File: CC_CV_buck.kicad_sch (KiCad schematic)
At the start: 29 parts, among them Q1 TIP42C, Q2 AO3400A, Q3 MMBT3906, U1 OPA2197xD, U2 INA194, U3 AOZ6605PI-1

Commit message: configure gitignore
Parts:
- U3: footprint aoz6605:SO8_EP1_AOS-M -> AOZ6605PI_1:SO8_EP1_AOS-L
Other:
- note added: "tie EN to a switch or something"
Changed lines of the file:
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@@
+		)
+	)
+	(text "tie EN to a switch or something "
+		(exclude_from_sim no)
+		(at 36.83 28.702 0)
+		(effects
+			(font
+				(size 1.27 1.27)
+			)
 		)
 	)
@@
 			)
 		)
-		(property "Footprint" "aoz6605:SO8_EP1_AOS-M"
+		(property "Footprint" "AOZ6605PI_1:SO8_EP1_AOS-L"
 			(at 64.77 41.91 0)
 			(effects

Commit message: did a bunch of stuff
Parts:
- added C12: 100n, symbol Device:C
- added C13, C14, C15, C16, C17: tbd, symbol Device:C
- added R11, R12, R13, R14, R15: tbd, symbol Device:R_US
- added RV1, RV2: tbd, symbol Device:R_Potentiometer_US
- added SW1: SW_SPDT_312, symbol Switch:SW_SPDT_312
- C11: value tbd -> 150u
- C5: value C_Small -> 100n
- R1, R2: value R_Small_US -> tbd
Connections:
- net GND: now also R2.2, U1.4 (V-), C12.2, C13.2, C14.2, C15.2, C16.2, C17.2, R14.1
- net at C2.1, R3.1, U1.2 (-): now also R13.1, R14.2
- net at Q1.2 (C), R10.1: now also C10.1, C11.1
- net at Q1.3 (E): now also L1.2, R1.1, C13.1, C14.1, C15.1, R11.1
- net VSET: now reaches U1.3 (+)
- net at R1.2, R2.1: now also SW1.2 (C)
- net at U3.2 (EN), U3.3 (VIN): now also C16.1, C17.1
- net at U3.8 (FB): now also SW1.1 (B)
- net ISET: now reaches U1.5 (+)
- net at C3.1, R4.1, U1.6 (-): now also R15.2
- net at Q3.1 (B): now also R12.1
- net at Q3.2 (E): now also R11.2
- net at Q3.3 (C), R9.1: now also SW1.3 (A)
- net at U2.1: now also R15.1
- net at R10.4: now also R13.2
- net at U1.8 (V+): now also C12.1
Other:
- note added: "300 kHz BW"
- note added: "500 mV / A"
- note added: "CC"
- note added: "CV"
- note added: "Vdo = Vfb_buck*(R11/R9)+ Veb"
- note added: "todo: find connectors for input, buck and LDO output figure out pot voltage ranges finalize Vin (~13V) and Vcc for control loop design buck LEDs for power, and CC/CV figure out better way to disconnect LDO and buck find shunt"
- moved on the sheet: C1, C10, C11, C2, C3, C4, C5, C6, C7, C8, C9, D1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

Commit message: added block terminals
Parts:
- removed SW1: SW_SPDT_312, symbol Switch:SW_SPDT_312
- added J1, J2, J3: ~, symbol Connector:Screw_Terminal_01x02
- added R16, R17: 0, symbol Device:R_Small_US
- C9: value tbd -> 1u
- R11: value tbd -> 10k
- R12: value tbd -> 1k
- R9: value tbd -> 15k
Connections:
- net GND: now also J1.2 (Pin_2), J2.2 (Pin_2), J3.2 (Pin_2)
- net at U3.8 (FB): now also R16.1, R17.1
- net at R1.2, R2.1: now also R16.2
- net at Q3.3 (C), R9.1: now also R17.2
- net VOUT_BUCK: now reaches C13.1, C14.1, L1.2, R1.1, R11.1
- net VOUT_BUCK: now also J1.1 (Pin_1); no longer C15.1, Q1.3 (E)
- net VOUT_LDO: now reaches R10.4, R13.2
- net VOUT_LDO: now also R12.2, J3.1 (Pin_1)
- new net VIN_LDO: C15.1, J2.1 (Pin_1), Q1.3 (E)
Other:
- note added: "0-10V 0-5A"
- note added: "connect J1 and J2 externally"
- note added: "todo: find connector for input figure out pot voltage ranges finalize Vin (~13V) and Vcc for control loop design buck LEDs for power, and CC/CV Make R1 and R2 a pot?"
- note removed: "todo: find connectors for input, buck and LDO output figure out pot voltage ranges finalize Vin (~13V) and Vcc for control loop design buck LEDs for power, and CC/CV figure out better way to disconnect LDO and buck find shunt"
- moved on the sheet: C1, C10, C11, C12, C15, C2, C3, C4, D1, Q1, Q2, Q3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

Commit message: buncha stuff
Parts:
- removed R10: 10m, symbol Device:R_Shunt_US
- added C18, C20: tbd, symbol Device:C
- added C19: 1u, symbol Device:C
- added D2: ZMMxx, Diode_SMD:D_MiniMELF_Handsoldering, symbol Diode:ZMMxx
- added J4: ~, symbol Connector:Screw_Terminal_01x02
- added Q4: MMBT3904, Package_TO_SOT_SMD:SOT-23, symbol Transistor_BJT:MMBT3904
- added R10: 10m, symbol Device:R_US
- added R18: 1k, symbol Device:R_US
- added R19: 330, symbol Device:R_US
- C11: value 150u -> tbd
- C16, C17: value tbd -> 4u7
- L1: value L -> 10u
- R13, R14: value tbd -> 500
- R6: value tbd -> 1k
- R7: value tbd -> 1
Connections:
- net GND: now also C10.2, C11.2, C18.2, C19.2, D2.2 (A), J4.2 (Pin_2), R18.2
- net VOUT_LDO: now also U2.4 (-), C20.1, R10.2
- net at C2.1, R13.1, R14.2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: now also C20.2
- net P13V0: now reaches C16.1, C17.1, U3.2 (EN), U3.3 (VIN)
- net P13V0: now also C18.1, J4.1 (Pin_1), Q4.3 (C), R19.1
- net at C10.1, C11.1, Q1.2 (C): now also U2.3 (+), R10.1
- net Vcc: now reaches C12.1, U1.8 (V+)
- net Vcc: now also R6.2, C19.1, Q4.2 (E), R18.1
- new net: D2.1 (K), Q4.1 (B), R19.2
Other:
- note added: "10V"
- note added: "13V in"
- note added: "need soft start / EN on LDO"
- moved on the sheet: C17

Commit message: uhh like alot of stuff
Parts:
- removed R1: tbd, symbol Device:R_Small_US
- added C21: 100n, Capacitor_SMD:C_0805_2012Metric_Pad1.18x1.45mm_HandSolder, symbol Device:C
- added C22: tbd, Capacitor_THT:CP_Radial_D8.0mm_P3.50mm, symbol Device:C_Polarized_US
- added C23: tbd, Capacitor_SMD:C_1210_3225Metric_Pad1.33x2.70mm_HandSolder, symbol Device:C
- added R20, R21: 0, Resistor_SMD:R_0805_2012Metric_Pad1.20x1.40mm_HandSolder, symbol Device:R_US
- added R22: 1k, Resistor_SMD:R_0805_2012Metric_Pad1.20x1.40mm_HandSolder, symbol Device:R_US
- added RV3: 20k, potentiometer:POT_PTN16-A20120K1B1, symbol Device:R_Potentiometer_US
- C1, C12, C15, C16, C17, C18, C19, C2, C20, C3, C4, C5, C6, C7, C8, C9: footprint (none) -> Capacitor_SMD:C_0805_2012Metric_Pad1.18x1.45mm_HandSolder
- C10, C13, C14: footprint (none) -> Capacitor_SMD:C_1210_3225Metric_Pad1.33x2.70mm_HandSolder
- C11: footprint (none) -> Capacitor_THT:CP_Radial_D8.0mm_P3.50mm
- J1, J2, J3, J4: footprint (none) -> TerminalBlock:TerminalBlock_Xinya_XY308-2.54-2P_1x02_P2.54mm_Horizontal
- L1: footprint (none) -> 10uH_inductor:L_Abracon_ASPI-1040HI
- R10, R11, R12, R15, R16, R17, R18, R19, R3, R4, R5, R6, R7, R8, R9: footprint (none) -> Resistor_SMD:R_0805_2012Metric_Pad1.20x1.40mm_HandSolder
- R13, R14: value 500 -> tbd; footprint (none) -> Resistor_SMD:R_0805_2012Metric_Pad1.20x1.40mm_HandSolder
- R2: value tbd -> 1k; footprint (none) -> Resistor_SMD:R_0805_2012Metric_Pad1.20x1.40mm_HandSolder
- RV1, RV2: footprint (none) -> potentiometer:POT_PTN16-A20120K1B1
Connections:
- net GND: now also R14.2, C21.2, C22.2, C23.2, R22.1; no longer R14.1
- net VOUT_BUCK: now also RV3.1
- net VOUT_LDO: now also R13.1; no longer R13.2
- net Vcc: now also U2.5 (V+), C21.1
- net V_SNS: now reaches C2.1, C20.2, R3.1, U1.2 (-)
- net V_SNS: now also R13.2, R14.1; no longer R13.1, R14.2
- net at C1.2, C2.2, U1.1: now also R21.1; no longer D1.2
- net BUCK_FB: now reaches R16.1, R17.1, U3.8 (FB)
- net at R16.2, R2.1: now also RV3.2, RV3.3
- net at C3.2, C4.2, U1.7: now also R20.1; no longer D1.1
- net I_SNS: now reaches R15.1, U2.1
- net BUCK_COMP: now reaches C7.1, R8.1, U3.7 (COMP)
- net BUCK_SS: now reaches C6.1, U3.1 (SS)
- net at C10.1, C11.1, Q1.2 (C)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: now also C22.1, C23.1, R22.2
- net BST: now reaches C5.1, U3.5 (BST)
- net BUCK_VCC: now reaches C9.1, U3.6 (VCC)
- net SW: now reaches C5.2, L1.1, U3.9 (LX)
- new net: D1.1, R20.2
- new net: D1.2, R21.2
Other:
- note added: "How much Cout on buck?"
- note added: "Seems like LDO should get most of the bulk cap"
- note added: "bleeder"
- note added: "use jumpers instead?"
- note added: "~9.4v"
- moved on the sheet: C10, C11, R10, R2, U2

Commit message: sorta finalize component placement as well as schematic
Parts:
- removed D2: ZMMxx, Diode_SMD:D_MiniMELF_Handsoldering, symbol Diode:ZMMxx
- removed R16, R17: 0, Resistor_SMD:R_0805_2012Metric_Pad1.20x1.40mm_HandSolder, symbol Device:R_Small_US
- removed R20, R21: 0, Resistor_SMD:R_0805_2012Metric_Pad1.20x1.40mm_HandSolder, symbol Device:R_US
- added C24, C25: 1u, Capacitor_SMD:C_0805_2012Metric_Pad1.18x1.45mm_HandSolder, symbol Device:C
- added C26: 4u7, Capacitor_SMD:C_0805_2012Metric_Pad1.18x1.45mm_HandSolder, symbol Device:C
- added C27: tbd, Capacitor_SMD:C_0805_2012Metric_Pad1.18x1.45mm_HandSolder, symbol Device:C
- added D2, D3: MMSZ5240BT1G, Diode_SMD:D_SOD-123, symbol Device:D_Zener
- added D4, D5: LED, symbol Device:LED
- added J5, J6, J7, J8: Conn_01x02_Pin, Connector_PinHeader_1.27mm:PinHeader_1x02_P1.27mm_Vertical, symbol Connector:Conn_01x02_Pin
- added R1, R16, R17: 10k, Resistor_SMD:R_0805_2012Metric_Pad1.20x1.40mm_HandSolder, symbol Device:R_US
- added U4: CSD25402Q3A, Package_SON:VSON-8_3.3x3.3mm_P0.65mm_NexFET, symbol Transistor_FET:CSD25402Q3A
- C18: value tbd -> 4u7
- RV1, RV2: value tbd -> 20k
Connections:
- net BUCK_FB: now also J7.2 (Pin_2), J8.2 (Pin_2)
- net GND: now also RV1.3, RV2.3, C24.2, C25.2, C26.2, D2.2 (A), R1.2
- net ISET: now also RV2.2, C25.1
- net I_SNS: now also C27.2
- net P13V0: now also C26.1, D3.1 (K), U4.5 (S); no longer J4.1 (Pin_1)
- net VSET: now also RV1.2, C24.1
- net Vcc: now also RV1.1, RV2.1, D4.2 (A), D5.2 (A)
- net CV_out: now reaches C1.2, C2.2, U1.1
- net CV_out: now also J5.1 (Pin_1), R16.2
- net at R2.1, RV3.2, RV3.3: now also J8.1 (Pin_1)
- net CC_out: now reaches C3.2, C4.2, U1.7
- net CC_out: now also J6.1 (Pin_1), R17.2
- net at D1.1: now also J6.2 (Pin_2)
- net at D1.2: now also J5.2 (Pin_2)
- net at C3.1, R15.2, R4.1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: now also C27.1
- net at Q4.1 (B), R19.2: now also D2.1 (K)
- net at Q3.3 (C), R9.1: now also J7.1 (Pin_1)
- new net: D3.2 (A), R1.1, U4.4 (G)
- new net: D4.1 (K), R16.1
- new net: D5.1 (K), R17.1
- new net VIN: J4.1 (Pin_1), U4.1 (D), U4.2 (D), U4.3 (D)
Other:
- note added: "CC/CV Indication"
- note added: "Power input / RPP"
- note added: "find LED fp investigate loop gain for CC buck Cout!"
- note removed: "need soft start / EN on LDO"
- note removed: "todo: find connector for input figure out pot voltage ranges finalize Vin (~13V) and Vcc for control loop design buck LEDs for power, and CC/CV Make R1 and R2 a pot?"
- note removed: "use jumpers instead?"
- moved on the sheet: C1, C10, C11, C12, C13, C14, C15, C16, C17, C19, C2, C20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

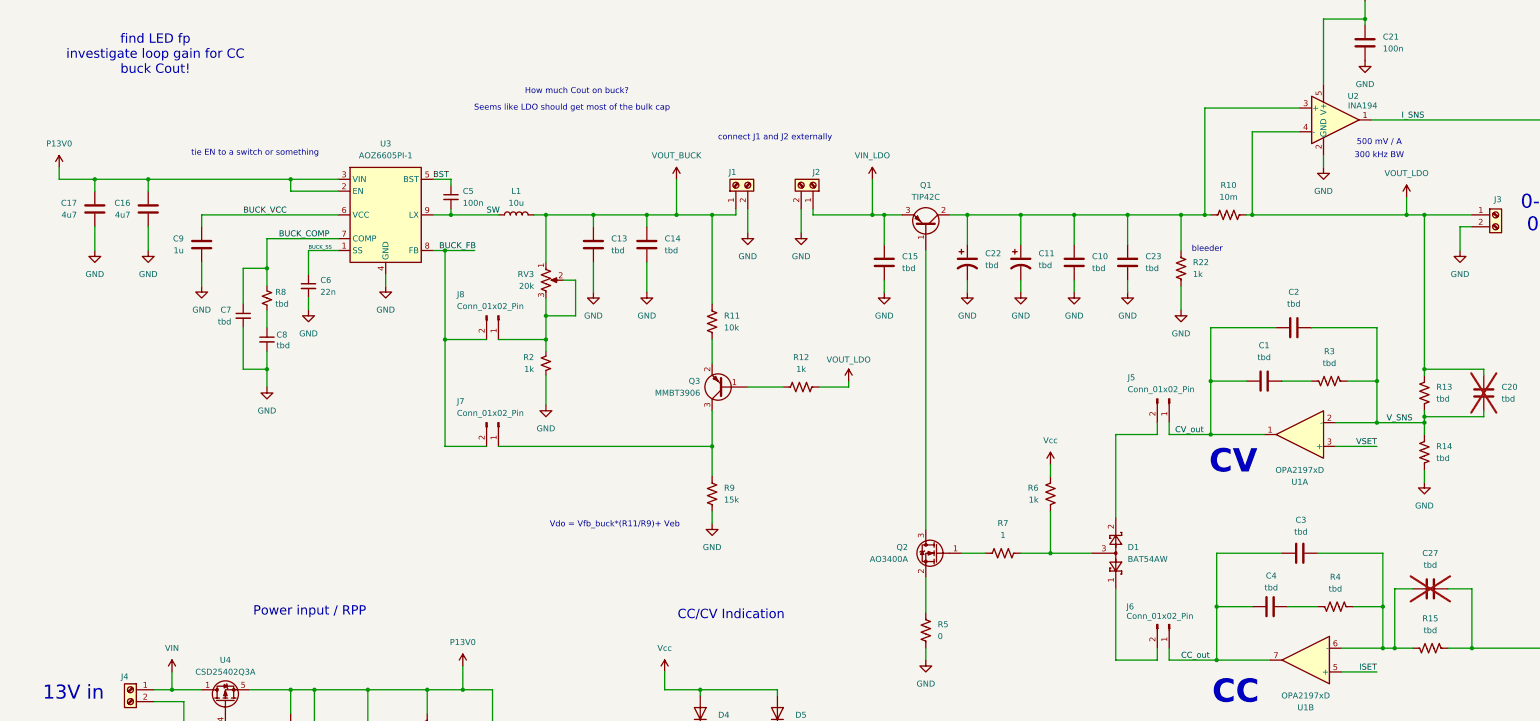
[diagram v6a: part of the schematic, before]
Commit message: add comp values for LDO, mess with layout a bit to see MH placement
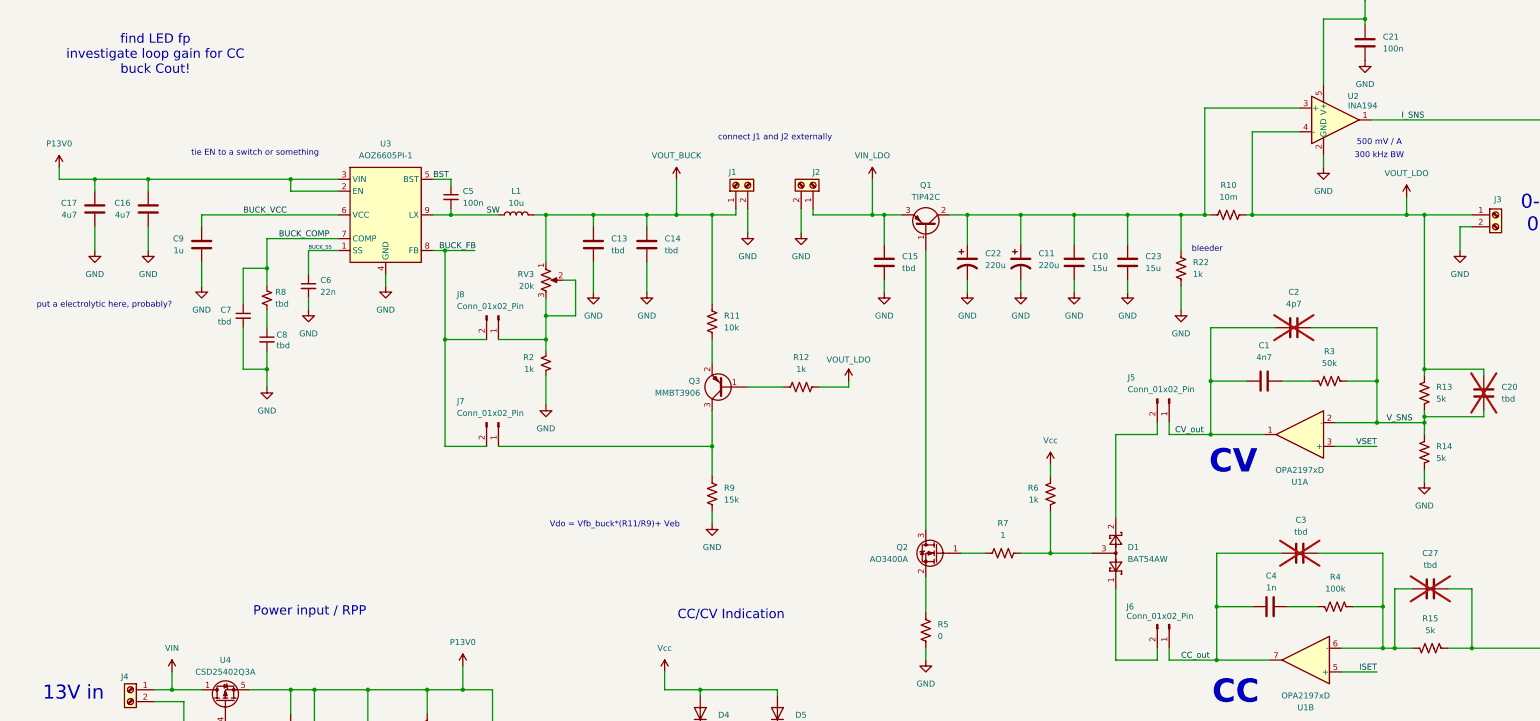
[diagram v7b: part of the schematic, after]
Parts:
- C1: value tbd -> 4n7
- C10, C23: value tbd -> 15u
- C11, C22: value tbd -> 220u
- C2: value tbd -> 4p7; now not fitted
- C3: now not fitted
- C4: value tbd -> 1n
- D4, D5: footprint (none) -> LED_SMD:LED_0603_1608Metric
- R13, R14, R15: value tbd -> 5k
- R3: value tbd -> 50k
- R4: value tbd -> 100k
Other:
- note added: "put a electrolytic here, probably?"
- note removed: "How much Cout on buck?"
- note removed: "Seems like LDO should get most of the bulk cap"
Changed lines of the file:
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@@
 		)
 	)
-	(text "Seems like LDO should get most of the bulk cap"
-		(exclude_from_sim no)
-		(at 130.048 48.26 0)
-		(effects
-			(font
-				(size 1.27 1.27)
-			)
-		)
-	)
 	(text "0-10V\n0-5A"
 		(exclude_from_sim no)
@@
 		)
 	)
-	(text "How much Cout on buck? "
+	(text "put a electrolytic here, probably?"
 		(exclude_from_sim no)
-		(at 131.064 44.704 0)
+		(at 29.972 90.424 0)
 		(effects
 			(font
@@
 		(in_bom yes)
 		(on_board yes)
-		(dnp no)
+		(dnp yes)
 		(fields_autoplaced yes)
 		(property "Reference" "C2"
@@
 			)
 		)
-		(property "Value" "tbd"
+		(property "Value" "4p7"
 			(at 284.48 90.17 90)
 			(effects
@@
 			)
 		)
-		(property "Value" "tbd"
+		(property "Value" "5k"
 			(at 314.96 123.1899 0)
 			(effects
@@
 			)
 		)
-		(property "Value" "tbd"
+		(property "Value" "5k"
 			(at 313.69 160.02 90)
 			(effects
@@
 		(in_bom yes)
 		(on_board yes)
-		(dnp no)
+		(dnp yes)
 		(property "Reference" "C3"
 			(at 286.004 136.398 90)
@@
 			)
 		)
-		(property "Value" "tbd"
+		(property "Value" "4n7"
 			(at 278.13 101.6 90)
 			(effects
@@
 			)
 		)
-		(property "Value" "tbd"
+		(property "Value" "15u"
 			(at 241.3 82.5499 0)
 			(effects
@@
 			)
 		)
-		(property "Footprint" ""
+		(property "Footprint" "LED_SMD:LED_0603_1608Metric"
 			(at 173.99 177.8 0)
 			(effects
@@
 			)
 		)
-		(property "Value" "tbd"
+		(property "Value" "220u"
 			(at 229.87 81.9149 0)
 			(effects
@@
 			)
 		)
-		(property "Footprint" ""
+		(property "Footprint" "LED_SMD:LED_0603_1608Metric"
 			(at 157.48 177.8 0)
 			(effects
@@
 			)
 		)
-		(property "Value" "tbd"
+		(property "Value" "220u"
 			(at 218.44 81.9149 0)
 			(effects
@@
 			)
 		)
-		(property "Value" "tbd"
+		(property "Value" "1n"
 			(at 279.654 150.876 90)
 			(effects
@@
 			)
 		)
-		(property "Value" "tbd"
+		(property "Value" "15u"
 			(at 252.73 82.5499 0)
 			(effects
@@
 			)
 		)
-		(property "Value" "tbd"
+		(property "Value" "100k"
 			(at 293.37 151.13 90)
 			(effects
@@
 			)
 		)
-		(property "Value" "tbd"
+		(property "Value" "5k"
 			(at 314.96 110.4899 0)
 			(effects
@@
 			)
 		)
-		(property "Value" "tbd"
+		(property "Value" "50k"
 			(at 292.1 102.87 90)
 			(effects

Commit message: more or less done w/ schematic and component placement
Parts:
- removed C14: tbd, Capacitor_SMD:C_1210_3225Metric_Pad1.33x2.70mm_HandSolder, symbol Device:C
- added C14: 220u, Capacitor_THT:CP_Radial_D8.0mm_P3.50mm, symbol Device:C_Polarized_US
- added H1, H2, H3, H4: MountingHole_Pad, MountingHole:MountingHole_2.2mm_M2_ISO7380_Pad, symbol Mechanical:MountingHole_Pad
- C13: value tbd -> 15u
- C15: value tbd -> 15u; footprint Capacitor_SMD:C_0805_2012Metric_Pad1.18x1.45mm_HandSolder -> Capacitor_SMD:C_1210_3225Metric_Pad1.33x2.70mm_HandSolder
- C16, C17: value 4u7 -> 15u; footprint Capacitor_SMD:C_0805_2012Metric_Pad1.18x1.45mm_HandSolder -> Capacitor_SMD:C_1210_3225Metric_Pad1.33x2.70mm_HandSolder
- J1, J2, J3, J4: footprint TerminalBlock:TerminalBlock_Xinya_XY308-2.54-2P_1x02_P2.54mm_Horizontal -> TerminalBlock_Phoenix_MPT-0,5-2-2.54_1x02_P2.54mm_Horizontal
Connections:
- net GND: now also J3.1 (Pin_1), C14.2, H1.1, H2.1, H3.1, H4.1; no longer J3.2 (Pin_2)
- net VOUT_BUCK: now also C14.1
- net VOUT_LDO: now also J3.2 (Pin_2); no longer J3.1 (Pin_1)
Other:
- note removed: "find LED fp investigate loop gain for CC buck Cout!"
- note removed: "put a electrolytic here, probably?"
- moved on the sheet: C1, C10, C11, C12, C13, C18, C19, C2, C20, C21, C22, C23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
